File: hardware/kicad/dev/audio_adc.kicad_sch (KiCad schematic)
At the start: 37 parts, among them J301 KLP42X-61-WW_RR, U301 PCM1802DBR, U401 PCM1802DBR

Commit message: updated LED footprint
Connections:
- net IN1_L: now also J301.5, R302.1; no longer J301.2, R402.1
- net IN1_R: now also J301.6, R301.1; no longer J301.3, R401.1
- net IN2_L: now also J301.2, R402.1; no longer J301.5, R302.1
- net IN2_R: now also J301.3, R401.1; no longer J301.6, R301.1
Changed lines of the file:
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@@
 		)
 	)
-	(global_label "IN1_L"
+	(global_label "IN2_L"
 		(shape input)
 		(at 158.75 74.93 180)
@@
 		)
 	)
-	(global_label "IN2_R"
-		(shape input)
+	(global_label "IN1_R"
+		(shape output)
 		(at 182.88 34.29 0)
 		(fields_autoplaced yes)
@@
 		)
 	)
-	(global_label "IN1_R"
-		(shape input)
+	(global_label "IN2_R"
+		(shape output)
 		(at 143.51 36.83 180)
 		(fields_autoplaced yes)
@@
 		)
 	)
-	(global_label "IN1_L"
-		(shape input)
+	(global_label "IN2_L"
+		(shape output)
 		(at 143.51 34.29 180)
 		(fields_autoplaced yes)
@@
 		)
 	)
-	(global_label "IN2_L"
-		(shape input)
+	(global_label "IN1_L"
+		(shape output)
 		(at 182.88 31.75 0)
 		(fields_autoplaced yes)
@@
 		)
 	)
-	(global_label "IN2_L"
+	(global_label "IN1_L"
 		(shape input)
 		(at 25.4 74.93 180)
@@
 		)
 	)
-	(global_label "IN1_R"
+	(global_label "IN2_R"
 		(shape input)
 		(at 158.75 92.71 180)
@@
 		)
 	)
-	(global_label "IN2_R"
+	(global_label "IN1_R"
 		(shape input)
 		(at 25.4 92.71 180)

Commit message: updated bom
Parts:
- C302, C305, C402, C405: Mouser Part Number (none) -> 80-C1812C944J5JLCLTU
- U301, U401: Mouser Part Number (none) -> 595-PCM1802DBR
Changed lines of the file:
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@@
 			)
 		)
+		(property "Mouser Part Number" "80-C1812C944J5JLCLTU"
+			(at 52.07 74.93 90)
+			(effects
+				(font
+					(size 1.27 1.27)
+				)
+				(hide yes)
+			)
+		)
 		(pin "1"
 		)
@@
 			)
 		)
+		(property "Mouser Part Number" "80-C1812C944J5JLCLTU"
+			(at 52.07 92.71 90)
+			(effects
+				(font
+					(size 1.27 1.27)
+				)
+				(hide yes)
+			)
+		)
 		(pin "1"
 		)
@@
 			)
 		)
+		(property "Mouser Part Number" "595-PCM1802DBR"
+			(at 88.9 82.55 0)
+			(effects
+				(font
+					(size 1.27 1.27)
+				)
+				(hide yes)
+			)
+		)
 		(pin "13"
 		)
@@
 			)
 		)
+		(property "Mouser Part Number" "80-C1812C944J5JLCLTU"
+			(at 189.23 74.93 90)
+			(effects
+				(font
+					(size 1.27 1.27)
+				)
+				(hide yes)
+			)
+		)
 		(pin "1"
 		)
@@
 			)
 		)
+		(property "Mouser Part Number" "80-C1812C944J5JLCLTU"
+			(at 189.23 92.71 90)
+			(effects
+				(font
+					(size 1.27 1.27)
+				)
+				(hide yes)
+			)
+		)
 		(pin "1"
 		)
@@
 			(at 227.33 82.55 0)
 			(effects
+				(font
+					(size 1.27 1.27)
+				)
+				(hide yes)
+			)
+		)
+		(property "Mouser Part Number" "595-PCM1802DBR"
+			(at 227.33 82.55 0)
+			(effects

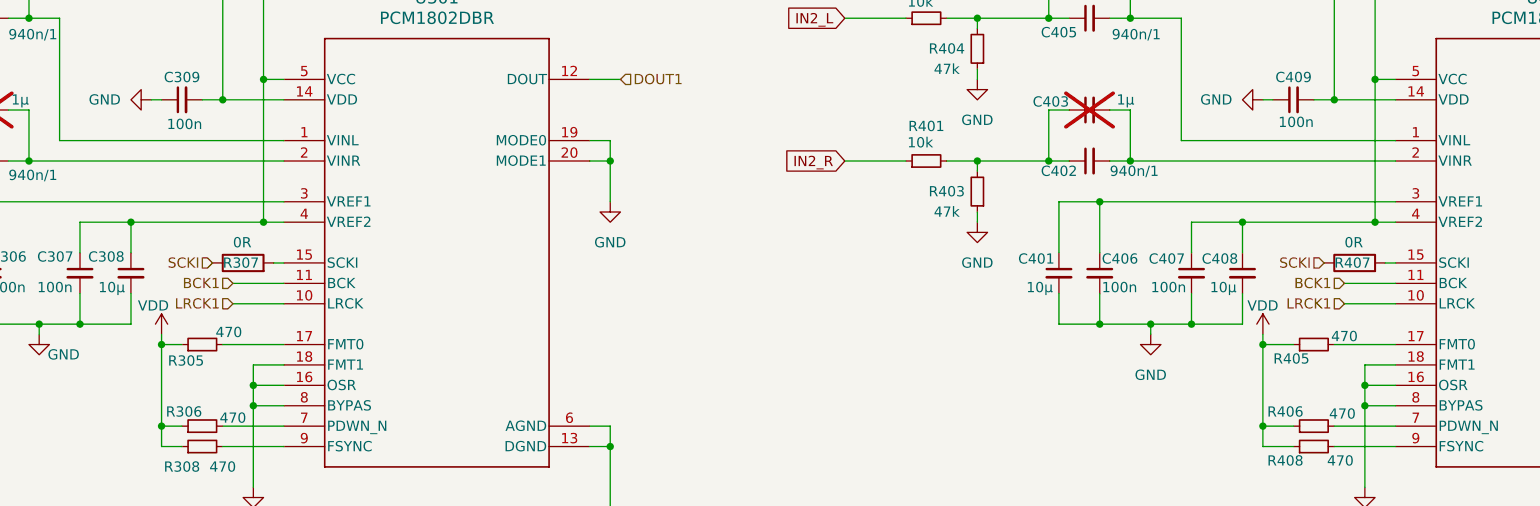
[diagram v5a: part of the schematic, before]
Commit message: optimized clock distribution
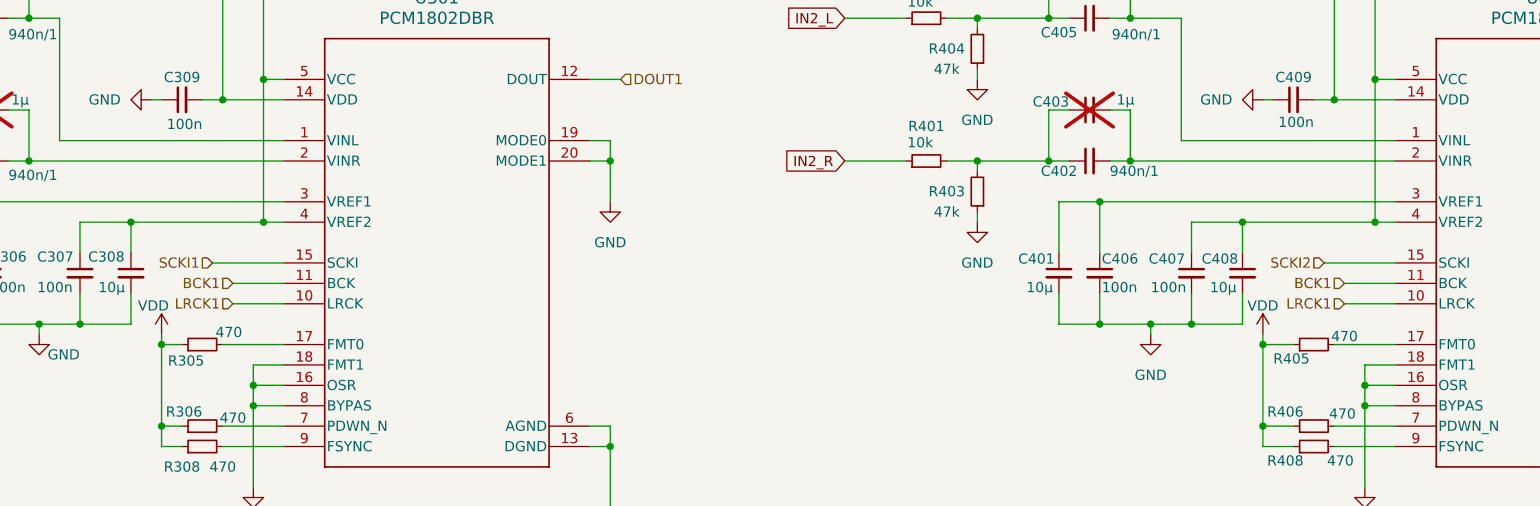
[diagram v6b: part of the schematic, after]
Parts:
- removed R307, R407: 0R, Resistor_SMD:R_0603_1608Metric, symbol Device:R
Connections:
- net SCKI2: now reaches U401.15 (SCKI)
- net SCKI1: now reaches U301.15 (SCKI)

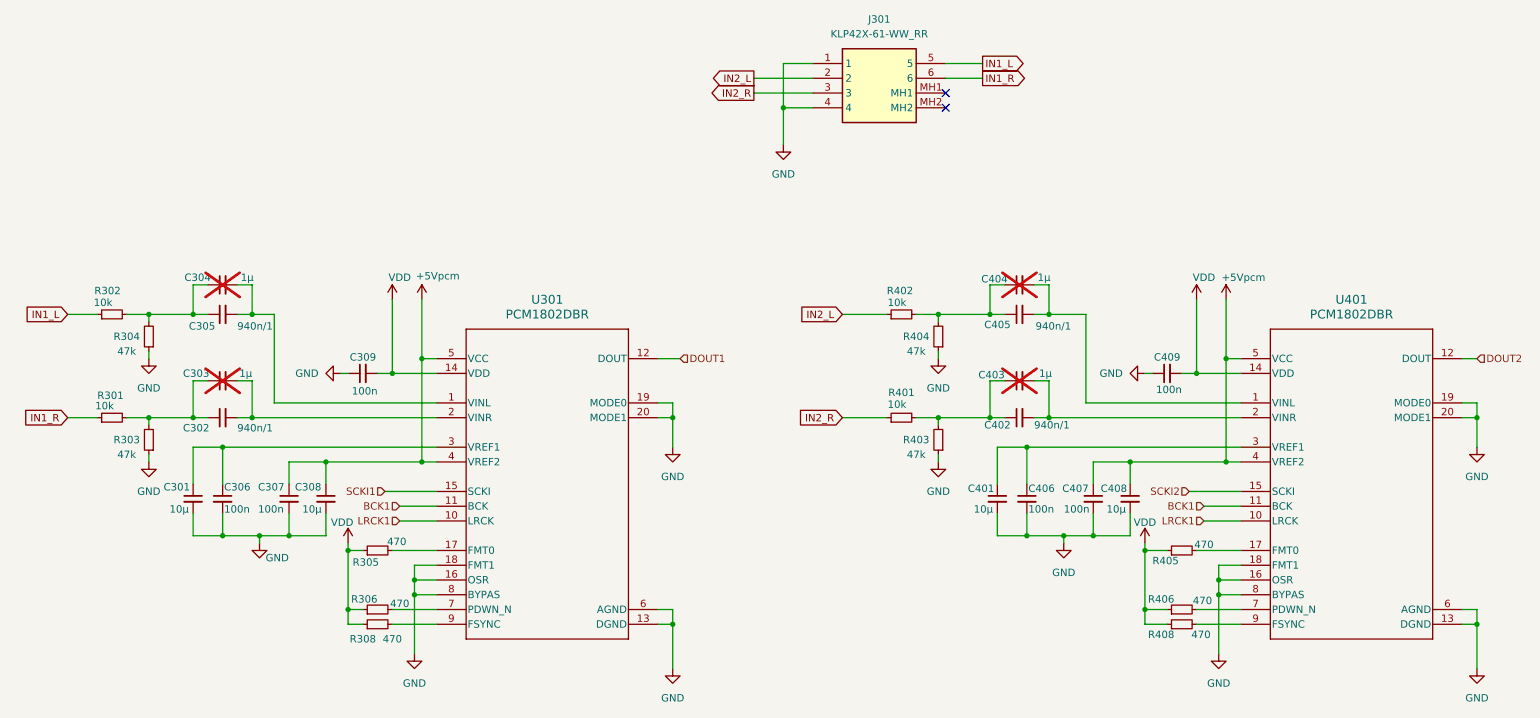
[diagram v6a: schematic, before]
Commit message: fixed zero adjust, more ferrit beads, silkscreen fixes
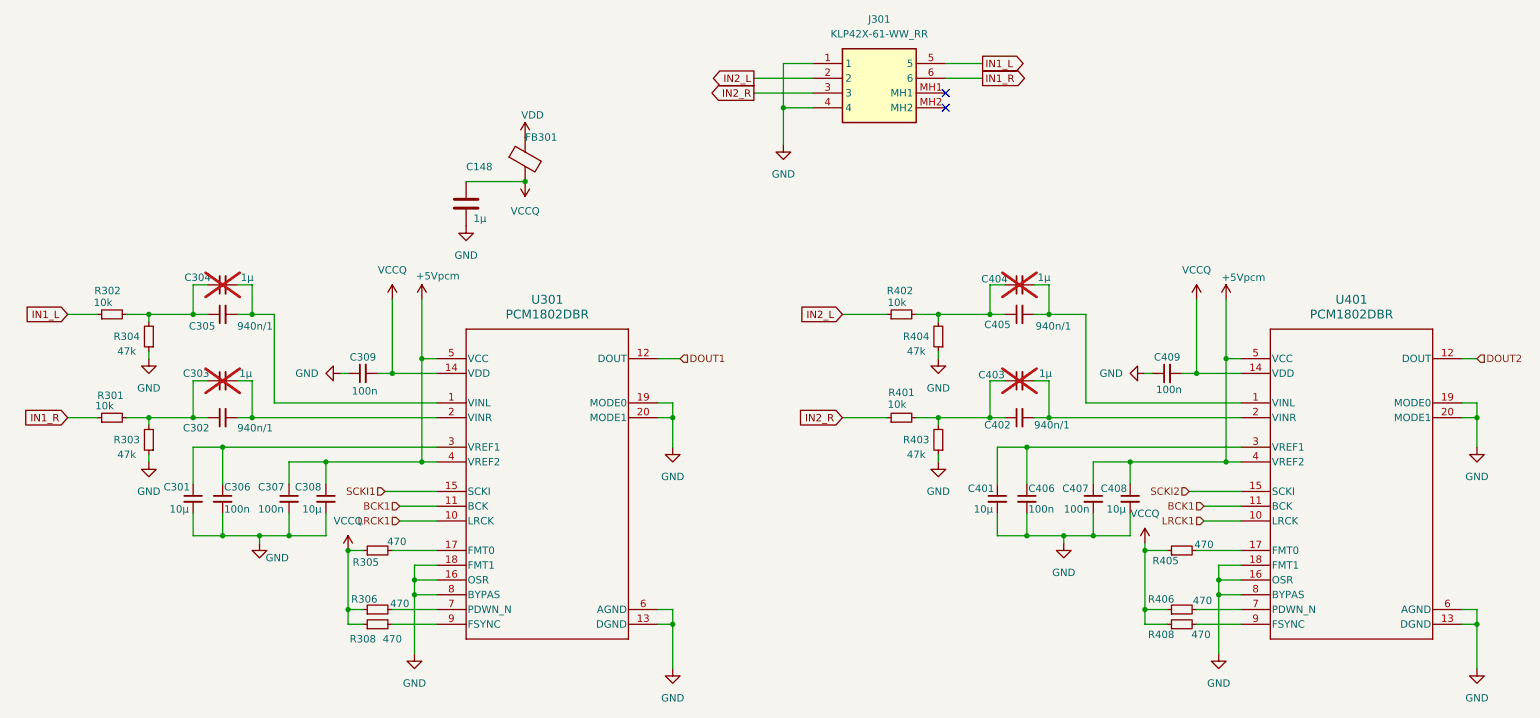
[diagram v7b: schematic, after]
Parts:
- added C148: 1µ, Capacitor_SMD:C_0603_1608Metric, symbol Device:C
- added FB301: 1k@100MHz,280@10MHz, Inductor_SMD:L_0603_1608Metric, symbol Device:FerriteBead
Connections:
- net GND: now also C148.2
- net VDD: now also FB301.1; no longer C309.2, C409.2, R305.1, R306.1, R308.1, R405.1, R406.1, R408.1, U301.14 (VDD), U401.14 (VDD)
- new net VCCQ: C148.1, C309.2, C409.2, FB301.2, R305.1, R306.1, R308.1, R405.1, R406.1, R408.1, U301.14 (VDD), U401.14 (VDD)
